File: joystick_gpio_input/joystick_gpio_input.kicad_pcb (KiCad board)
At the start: 2 copper layers, 23 x 46.6 mm, 22 parts, among them J1 Conn_01x06, J2 Conn_01x04, J3 Conn_01x15, J4 Conn_01x15_Male, J5 Conn_01x15_Male

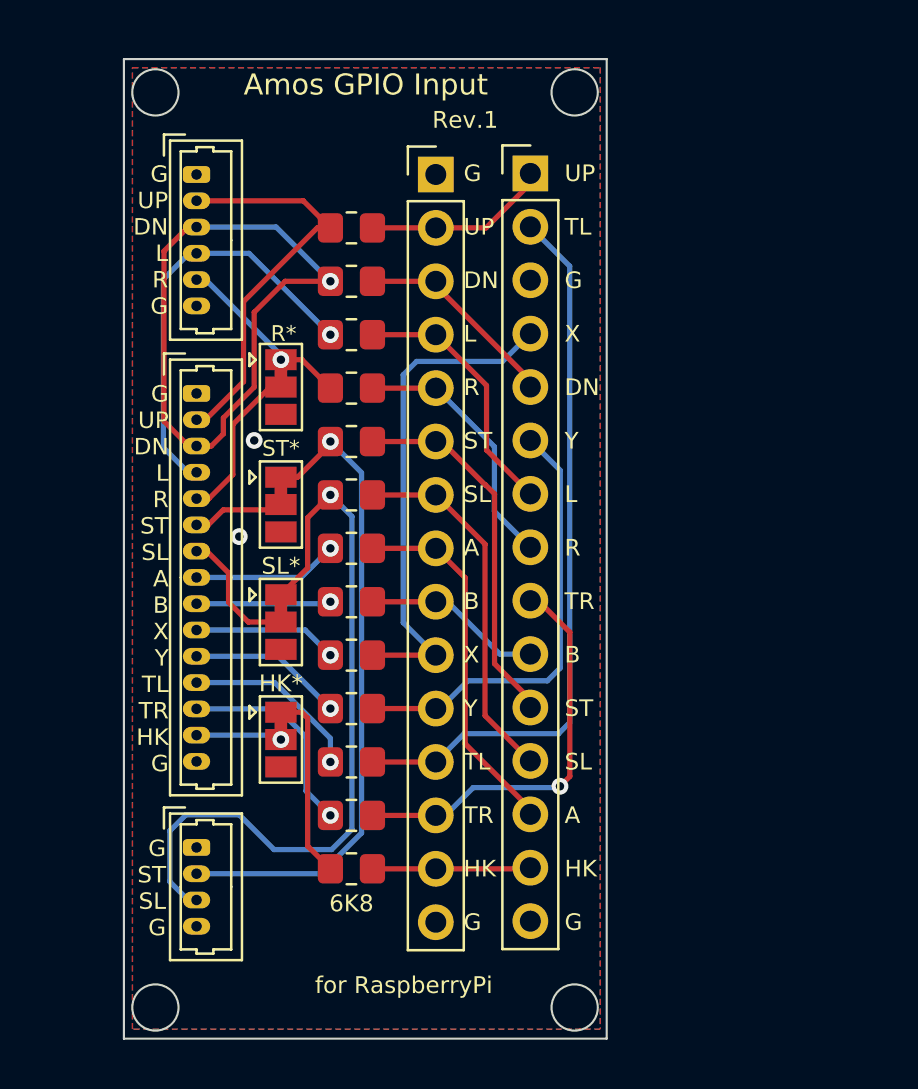
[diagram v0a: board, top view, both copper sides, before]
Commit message: gpio 입력 보드 점퍼 변경
Signed-off-by: Ju, Gyeong-min <jcmh74@gmail.com>
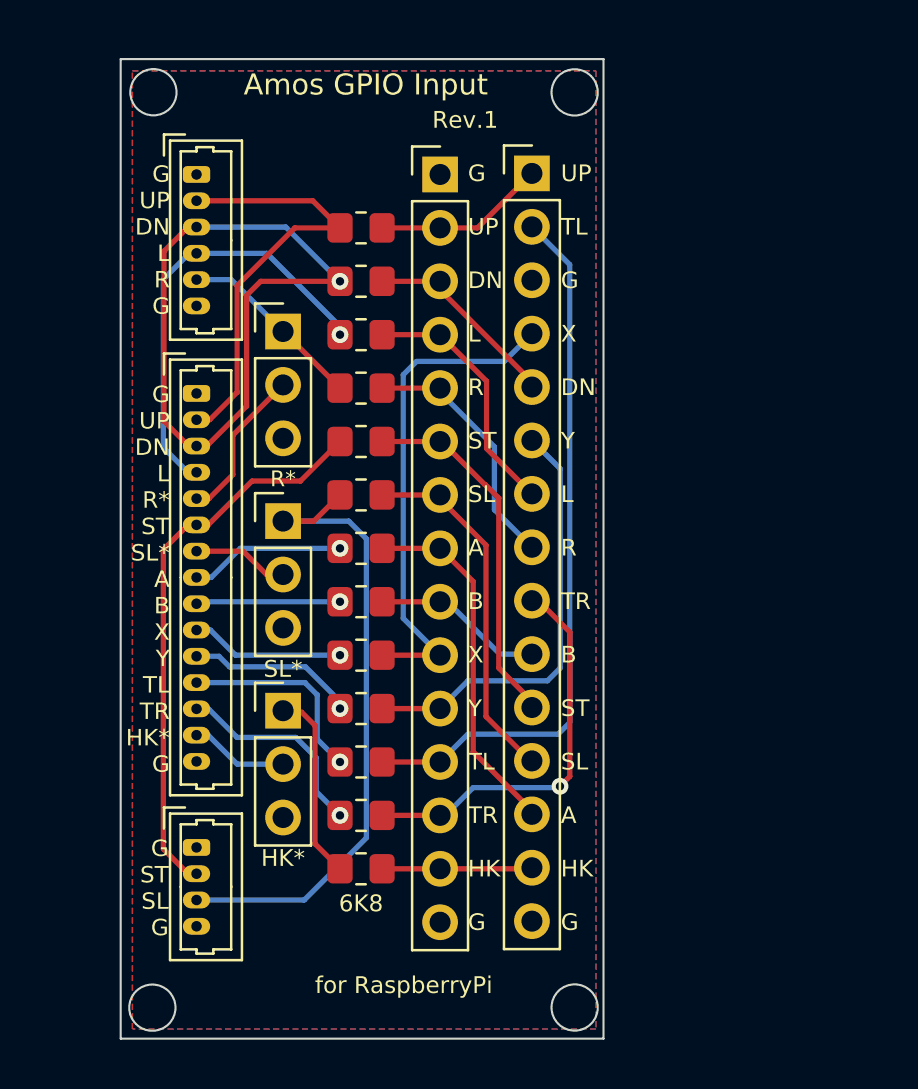
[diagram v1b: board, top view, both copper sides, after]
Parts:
- removed the JP2 at (137.2, 101.3)
- JP1: value SolderJumper_3_Bridged12 -> Conn_01x03; footprint Jumper:SolderJumper-3_P1.3mm_Bridged12_Pad1.0x1.5mm -> Connector_PinHeader_2.54mm:PinHeader_1x03_P2.54mm_Vertical
- JP2: renamed from JP3; value SolderJumper_3_Bridged12 -> Conn_01x03; footprint Jumper:SolderJumper-3_P1.3mm_Bridged12_Pad1.0x1.5mm -> Connector_PinHeader_2.54mm:PinHeader_1x03_P2.54mm_Vertical
- JP3: renamed from JP4; value SolderJumper_3_Bridged12 -> Conn_01x03; footprint Jumper:SolderJumper-3_P1.3mm_Bridged12_Pad1.0x1.5mm -> Connector_PinHeader_2.54mm:PinHeader_1x03_P2.54mm_Vertical
- moved JP2 4.80 mm to (137.3, 102.1), turned to 0 degrees
- moved JP1 2.64 mm to (137.3, 93.1), turned to 0 degrees
- moved JP3 1.38 mm to (137.3, 111.2), turned to 0 degrees
- moved R1 0.46 mm to (141.0, 88.2)
- moved R10 0.46 mm to (141.0, 111.0)
- moved R11 0.46 mm to (141.0, 113.6)
- moved R12 0.46 mm to (141.0, 116.1)
- moved R13 0.46 mm to (141.0, 118.7)
- moved R2 0.46 mm to (141.0, 90.7)
- moved R3 0.46 mm to (141.0, 93.3)
- moved R4 0.46 mm to (141.0, 95.8)
- moved R5 0.46 mm to (141.0, 98.3)
- moved R6 0.46 mm to (141.0, 100.9)
- moved R7 0.46 mm to (141.0, 103.4)
- moved R8 0.46 mm to (141.0, 106.0)
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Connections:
- J3 pad 6: /START_T -> /START
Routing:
- net /SELECT: track 36.2 -> 31.1 mm, vias 1 -> 0
- net /START_T: track 4.41 -> 0.00 mm
- net /START: track 31.0 -> 26.8 mm, vias 1 -> 0
- net /UP: track 19.3 -> 20.9 mm
- net /SELECT_T: track 6.23 -> 4.57 mm
- net /DOWN: track 31.7 -> 33.2 mm
- net /TL: track 8.59 -> 9.62 mm
- net /LEFT: track 20.1 -> 20.8 mm
- net /C_UP: track 8.86 -> 8.20 mm
- net /Y: track 7.40 -> 8.05 mm
- net /HK_T: track 4.10 -> 4.69 mm, vias 1 -> 0
- net /C_TR: track 19.5 -> 19.0 mm
- net /RIGHT: track 8.63 -> 8.96 mm, vias 1 -> 0
- net /GND: vias 2 -> 0
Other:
- outline, holes or cut-outs redrawn
- board text added: "G UP DN L R* ST SL* A B X Y TL TR HK* G"
- board text removed: "ST*"

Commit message: gpio input 보드 크기 조정
Signed-off-by: Ju, Gyeong-min <jcmh74@gmail.com>
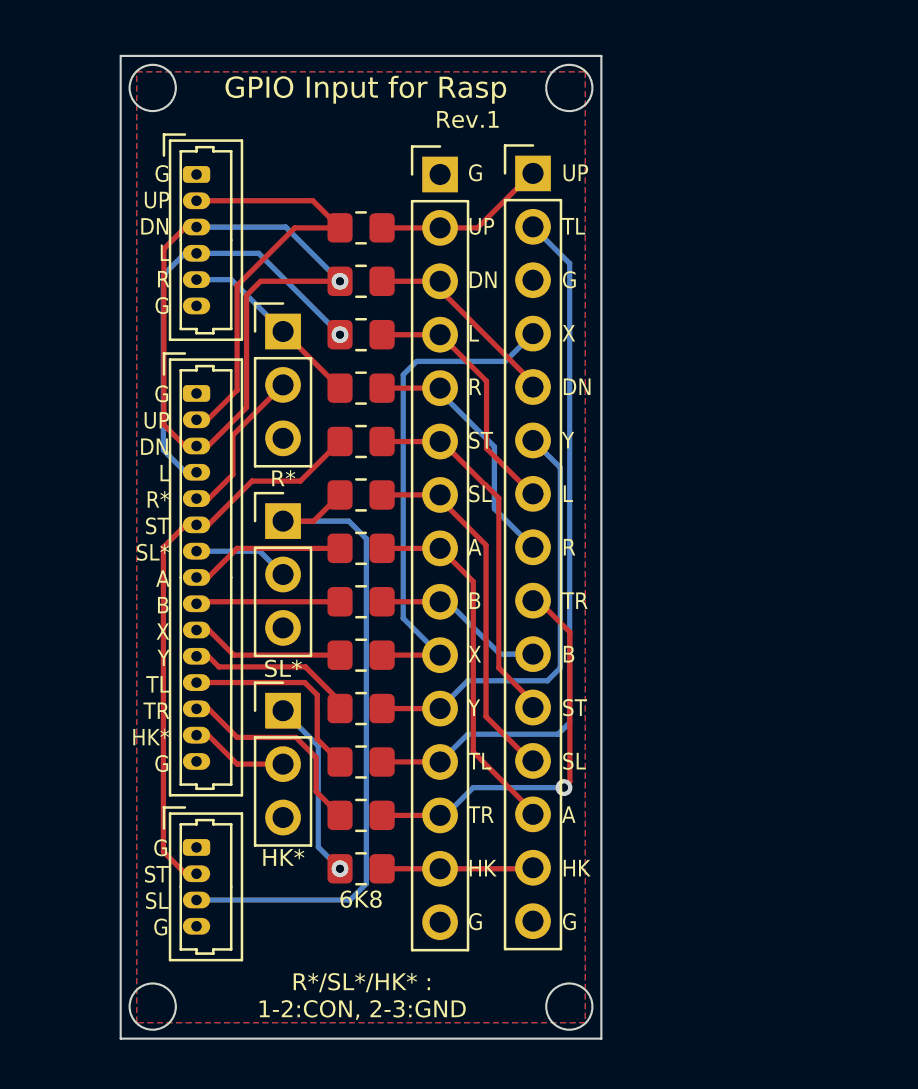
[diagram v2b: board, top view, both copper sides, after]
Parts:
- moved J5 0.05 mm to (149.1, 85.6)
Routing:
- net /SELECT: track 31.1 -> 32.3 mm
- net /HK: track 9.19 -> 8.64 mm, vias 0 -> 1
- net /Y: vias 1 -> 0
- net /X: vias 1 -> 0
- net /TR: vias 1 -> 0
- net /TL: vias 1 -> 0
- net /B: vias 1 -> 0
- net /A: vias 1 -> 0
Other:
- board size 23 x 46.6 mm -> 22.9 x 46.7 mm
- board text added: "GPIO Input for Rasp"
- board text added: "R*/SL*/HK* : 1-2:CON, 2-3:GND"
- board text removed: "Amos GPIO Input"
- board text removed: "for RaspberryPi"

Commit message: gpio 입력 보드 확장
Signed-off-by: Ju, Gyeong-min <jcmh74@gmail.com>
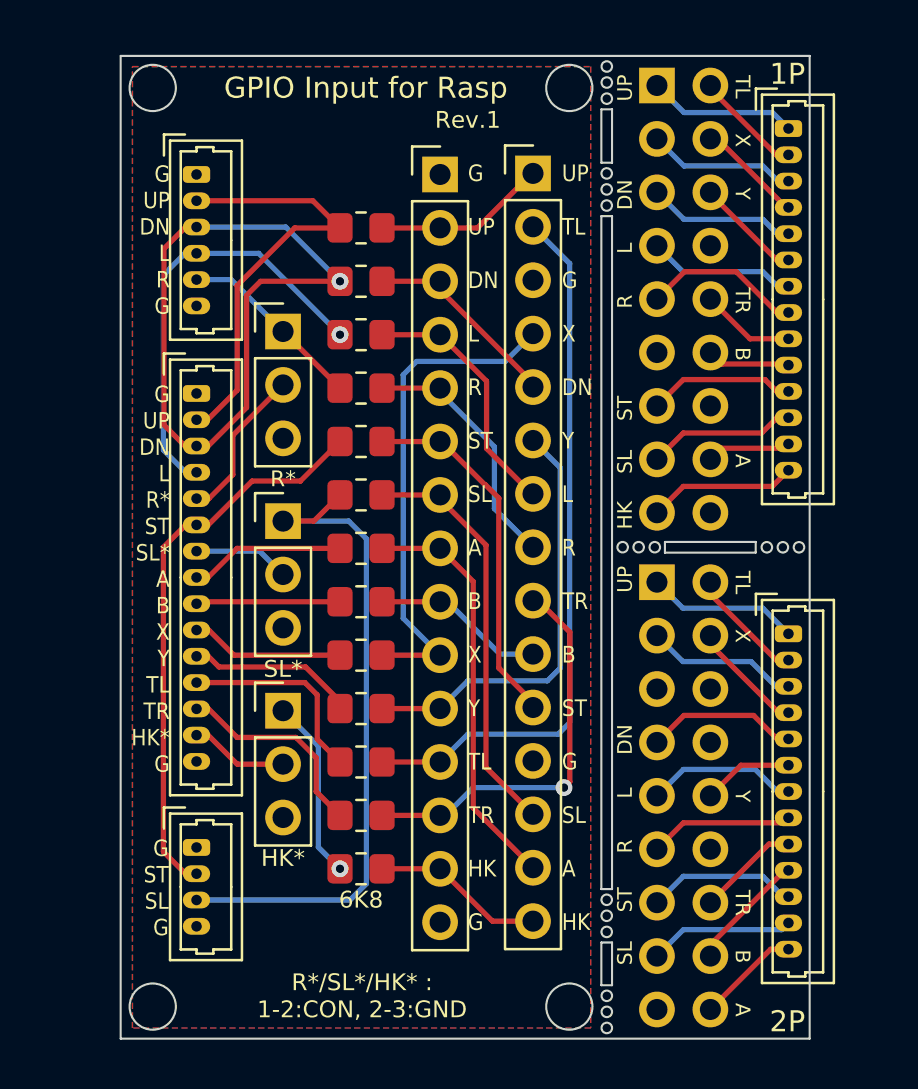
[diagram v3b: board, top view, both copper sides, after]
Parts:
- added J6: Conn_01x14, Connector_Molex:Molex_PicoBlade_53047-1410_1x14_P1.25mm_Vertical, F.Cu at (161.3, 83.5)
- added J7: Conn_01x13, Connector_Molex:Molex_PicoBlade_53047-1310_1x13_P1.25mm_Vertical, F.Cu at (161.3, 107.5)
- added J8: Conn_02x09_Odd_Even, Connector_PinSocket_2.54mm:PinSocket_2x09_P2.54mm_Vertical, B.Cu at (155.0, 81.4)
- added J9: Conn_02x09_Odd_Even, Connector_PinSocket_2.54mm:PinSocket_2x09_P2.54mm_Vertical, B.Cu at (155.0, 105.0)
- J4, J5: value Conn_01x15_Male -> Conn_01x15
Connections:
- J5 pad 12: /C_SELECT -> /GND
- J5 pad 13: /C_A -> /C_SELECT
- J5 pad 14: /C_HK -> /C_A
- J5 pad 15: /GND -> /C_HK
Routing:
- net /1P_RIGHT: track 0.00 -> 7.60 mm
- net /2P_UP: track 0.00 -> 7.27 mm
- net /2P_GND: track 0.00 -> 7.25 mm
- net /2P_DOWN: track 0.00 -> 7.25 mm
- net /2P_LEFT: track 0.00 -> 7.21 mm
- net /2P_START: track 0.00 -> 7.17 mm
- net /1P_UP: track 0.00 -> 7.10 mm
- net /1P_HK: track 0.00 -> 7.09 mm
- net /1P_GND: track 0.00 -> 7.08 mm
- net /1P_SELECT: track 0.00 -> 7.07 mm
- net /1P_DOWN: track 0.00 -> 7.07 mm
- net /1P_LEFT: track 0.00 -> 7.05 mm
- net /1P_START: track 0.00 -> 7.01 mm
- net /2P_SELECT: track 0.00 -> 6.91 mm
- net /2P_RIGHT: track 0.00 -> 6.87 mm
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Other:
- board size 22.9 x 46.7 mm -> 32.8 x 46.7 mm
- board text added: "1P"
- board text added: "2P"
- board text added: "A"
- board text added: "B"
- board text added: "DN"
- board text added: "HK"
- board text added: "L"
- board text added: "R"
- board text added: "SL"
- board text added: "ST"
- board text added: "TL"
- board text added: "TR"
- board text added: "UP"
- board text added: "UP TL G X DN Y L R TR B ST G SL A HK"
- board text added: "UP TL G X DN Y L R TR B ST SL A"
- board text added: "UP TL G X DN Y L R TR B ST SL A HK"
- board text added: "X"
- board text added: "Y"
- board text removed: "UP TL G X DN Y L R TR B ST SL A HK G"

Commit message: gpio 입력 보드 커넥터 1개씩 늘림
Signed-off-by: Ju, Gyeong-min <jcmh74@gmail.com>
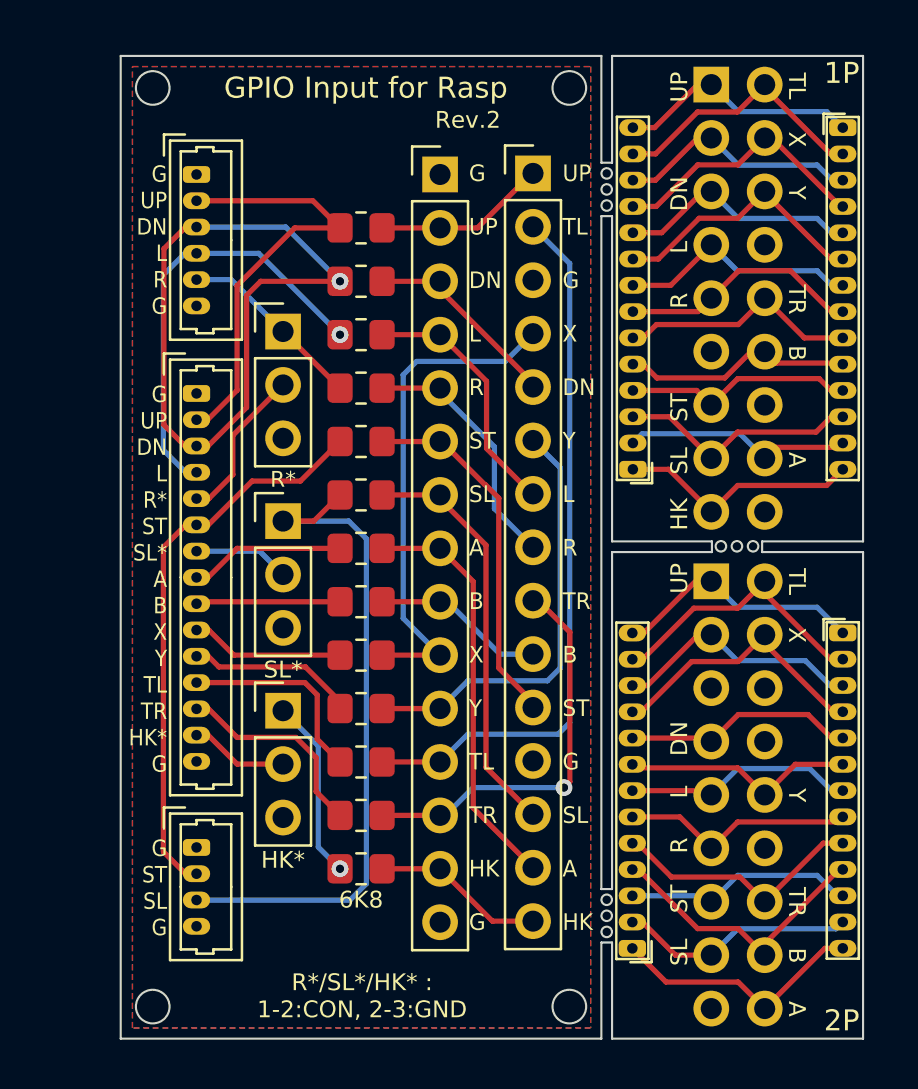
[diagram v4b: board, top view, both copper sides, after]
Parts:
- added J10: Conn_01x14, joystick_gpio_input_library:conn_ex_1x14_P1.25mm_Vertical, F.Cu at (153.9, 99.7)
- added J11: Conn_01x13, joystick_gpio_input_library:conn_ex_1x13_P1.25mm_Vertical, F.Cu at (153.9, 122.5)
- J8: renamed from J6; footprint Connector_Molex:Molex_PicoBlade_53047-1410_1x14_P1.25mm_Vertical -> joystick_gpio_input_library:conn_ex_1x14_P1.25mm_Vertical
- J9: renamed from J7; footprint Connector_Molex:Molex_PicoBlade_53047-1310_1x13_P1.25mm_Vertical -> joystick_gpio_input_library:conn_ex_1x13_P1.25mm_Vertical
- moved J6 2.58 mm to (157.6, 81.4)
- moved J7 2.58 mm to (157.6, 105.0)
- moved J8 2.58 mm to (163.9, 83.4)
- moved J9 2.58 mm to (163.9, 107.4)
- renumbered J8 to J6, J9 to J7
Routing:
- net /2P_B: track 5.72 -> 13.7 mm
- net /2P_TL: track 5.58 -> 13.4 mm
- net /2P_X: track 5.48 -> 13.3 mm
- net /1P_TL: track 5.17 -> 12.8 mm
- net /1P_X: track 5.06 -> 12.7 mm
- net /1P_Y: track 5.08 -> 12.7 mm
- net /2P_A: track 4.90 -> 12.4 mm
- net /2P_TR: track 4.87 -> 12.3 mm
- net /1P_B: track 3.96 -> 11.0 mm
- net /1P_TR: track 4.50 -> 11.5 mm
- net /1P_A: track 4.02 -> 11.0 mm
- net /2P_Y: track 4.32 -> 11.2 mm
- net /2P_UP: track 7.27 -> 12.0 mm
- net /2P_GND: track 7.25 -> 12.0 mm
- net /1P_UP: track 7.10 -> 11.7 mm
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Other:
- board size 32.8 x 46.7 mm -> 35.3 x 46.7 mm
- board text added: "Rev.2"
- board text removed: "Rev.1"

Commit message: Rev 2 설계
Signed-off-by: Ju, Gyeong-min <jcmh74@gmail.com>
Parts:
- added J12: Conn_01x15, Connector_PinHeader_2.54mm:PinHeader_1x15_P2.54mm_Vertical, F.Cu at (138.3, 85.6)
- J10: footprint joystick_gpio_input_library:conn_ex_1x14_P1.25mm_Vertical -> joystick_gpio_input_library:conn_ex_1x14_P1.25mm_Vertical_Left_Labeled; moved to B.Cu
- J11: footprint joystick_gpio_input_library:conn_ex_1x13_P1.25mm_Vertical -> joystick_gpio_input_library:conn_ex_1x13_P1.25mm_Vertical_Left_Labeled; moved to B.Cu
- J5: value Conn_01x15 -> Conn_01x14; footprint Connector_PinHeader_2.54mm:PinHeader_1x15_P2.54mm_Vertical -> joystick_gpio_input_library:conn_ex_1x14_P1.25mm_Vertical_Left_Labeled
- J8: footprint joystick_gpio_input_library:conn_ex_1x14_P1.25mm_Vertical -> joystick_gpio_input_library:conn_ex_1x14_P1.25mm_Vertical_Right_Labeled; moved to B.Cu
- J9: footprint joystick_gpio_input_library:conn_ex_1x13_P1.25mm_Vertical -> joystick_gpio_input_library:conn_ex_1x13_P1.25mm_Vertical_Right_Labeled; moved to B.Cu
- moved J10 16.6 mm to (154.3, 83.1), turned to -90 degrees
- moved J11 14.7 mm to (154.3, 107.7), turned to -90 degrees
- moved J5 9.72 mm to (151.1, 95.1), turned to -90 degrees
- moved J1 3.29 mm to (129.9, 85.6)
- moved J2 3.27 mm to (129.9, 117.6)
- moved J3 3.27 mm to (129.9, 96.0)
- moved JP1 3.03 mm to (134.3, 92.8)
- moved JP3 3.02 mm to (134.3, 111.3)
- moved JP2 3.01 mm to (134.3, 102.1)
- moved J4 1.08 mm to (145.8, 85.6)
- moved R1 1.08 mm to (142.0, 88.1)
- moved R10 1.08 mm to (142.0, 111.0)
- moved R11 1.08 mm to (142.0, 113.5)
- moved R12 1.08 mm to (142.0, 116.1)
- moved R13 1.08 mm to (142.0, 118.6)
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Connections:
- J10 pad 1: /1P_HK -> /1P_UP
- J10 pad 10: /1P_DOWN -> /1P_START
- J10 pad 11: /1P_X -> /1P_SELECT
- J10 pad 12: /1P_GND -> /1P_A
- J10 pad 13: /1P_TL -> /1P_GND
- J10 pad 14: /1P_UP -> /1P_HK
- J10 pad 2: /1P_A -> /1P_TL
- J10 pad 3: /1P_SELECT -> /1P_X
- J10 pad 4: /1P_START -> /1P_DOWN
- J10 pad 5: /1P_B -> /1P_Y
- J10 pad 6: /1P_TR -> /1P_LEFT
- J10 pad 8: /1P_LEFT -> /1P_TR
- J10 pad 9: /1P_Y -> /1P_B
- J11 pad 1: /2P_A -> /2P_UP
- J11 pad 10: /2P_X -> /2P_START
- J11 pad 11: /2P_GND -> /2P_SELECT
- J11 pad 12: /2P_TL -> /2P_A
- J11 pad 13: /2P_UP -> /2P_GND
- J11 pad 2: /2P_SELECT -> /2P_TL
- J11 pad 3: /2P_START -> /2P_X
- J11 pad 4: /2P_B -> /2P_DOWN
- J11 pad 5: /2P_TR -> /2P_Y
- J11 pad 6: /2P_RIGHT -> /2P_LEFT
- J11 pad 7: /2P_LEFT -> /2P_RIGHT
- J11 pad 8: /2P_Y -> /2P_TR
- J11 pad 9: /2P_DOWN -> /2P_B
- J5 pad 10: /C_B -> /C_START
- J5 pad 11: /C_START -> /C_SELECT
- J5 pad 12: /GND -> /C_A
- J5 pad 13: /C_SELECT -> /GND
- J5 pad 14: /C_A -> /C_HK
- J5 pad 3: /GND -> /C_X
- J5 pad 4: /C_X -> /C_DOWN
- J5 pad 5: /C_DOWN -> /C_Y
- J5 pad 6: /C_Y -> /C_LEFT
- J5 pad 7: /C_LEFT -> /C_RIGHT
- J5 pad 8: /C_RIGHT -> /C_TR
- J5 pad 9: /C_TR -> /C_B
- J6 pad 14: unconnected-(J6-Pin_14-Pad14) -> /1P_GND
- J6 pad 8: unconnected-(J6-Pin_8-Pad8) -> /1P_GND
- J7 pad 12: unconnected-(J7-Pin_12-Pad12) -> /2P_GND
- J7 pad 17: unconnected-(J7-Pin_17-Pad17) -> /2P_GND
- J7 pad 8: unconnected-(J7-Pin_8-Pad8) -> /2P_GND
- J8 pad 10: /1P_B -> /1P_START
- J8 pad 11: /1P_START -> /1P_SELECT
- J8 pad 12: /1P_SELECT -> /1P_A
- J8 pad 13: /1P_A -> /1P_GND
- J8 pad 3: /1P_GND -> /1P_X
- J8 pad 4: /1P_X -> /1P_DOWN
- J8 pad 5: /1P_DOWN -> /1P_Y
- J8 pad 6: /1P_Y -> /1P_LEFT
- J8 pad 7: /1P_LEFT -> /1P_RIGHT
- J8 pad 8: /1P_RIGHT -> /1P_TR
- J8 pad 9: /1P_TR -> /1P_B
- J9 pad 10: /2P_B -> /2P_START
- J9 pad 11: /2P_START -> /2P_SELECT
- J9 pad 12: /2P_SELECT -> /2P_A
- J9 pad 13: /2P_A -> /2P_GND
- J9 pad 3: /2P_GND -> /2P_X
- J9 pad 4: /2P_X -> /2P_DOWN
- J9 pad 5: /2P_DOWN -> /2P_Y
- J9 pad 6: /2P_Y -> /2P_LEFT
- J9 pad 7: /2P_LEFT -> /2P_RIGHT
- J9 pad 8: /2P_RIGHT -> /2P_TR
- J9 pad 9: /2P_TR -> /2P_B
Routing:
- net /GND: track 0.00 -> 108.1 mm
- net /2P_GND: track 12.0 -> 33.3 mm
- net /1P_GND: track 11.6 -> 26.3 mm
- net /C_A: track 19.8 -> 11.4 mm
- net /C_TL: track 34.0 -> 26.4 mm
- net /C_X: track 23.8 -> 16.3 mm
- net /C_SELECT: track 19.8 -> 12.8 mm
- net /DOWN: track 33.4 -> 26.9 mm, vias 1 -> 0
- net /C_B: track 8.21 -> 14.5 mm, vias 0 -> 1
- net /C_Y: track 20.6 -> 16.0 mm
- net /X: track 7.32 -> 11.8 mm
- net /B: track 6.86 -> 11.3 mm
- net /RIGHT: track 8.96 -> 13.3 mm
- net /A: track 7.40 -> 11.7 mm
- net /C_HK: track 8.21 -> 12.4 mm
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- removed copper zone on B.Cu, net /GND
- removed copper zone on F.Cu, net /GND
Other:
- board size 35.3 x 46.7 mm -> 39 x 47.5 mm
- board text added: "G"
- board text removed: "UP TL G X DN Y L R TR B ST G SL A HK"
- board text removed: "UP TL G X DN Y L R TR B ST SL A"
- board text removed: "UP TL G X DN Y L R TR B ST SL A HK"
